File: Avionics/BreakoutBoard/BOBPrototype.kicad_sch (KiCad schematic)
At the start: 0 parts

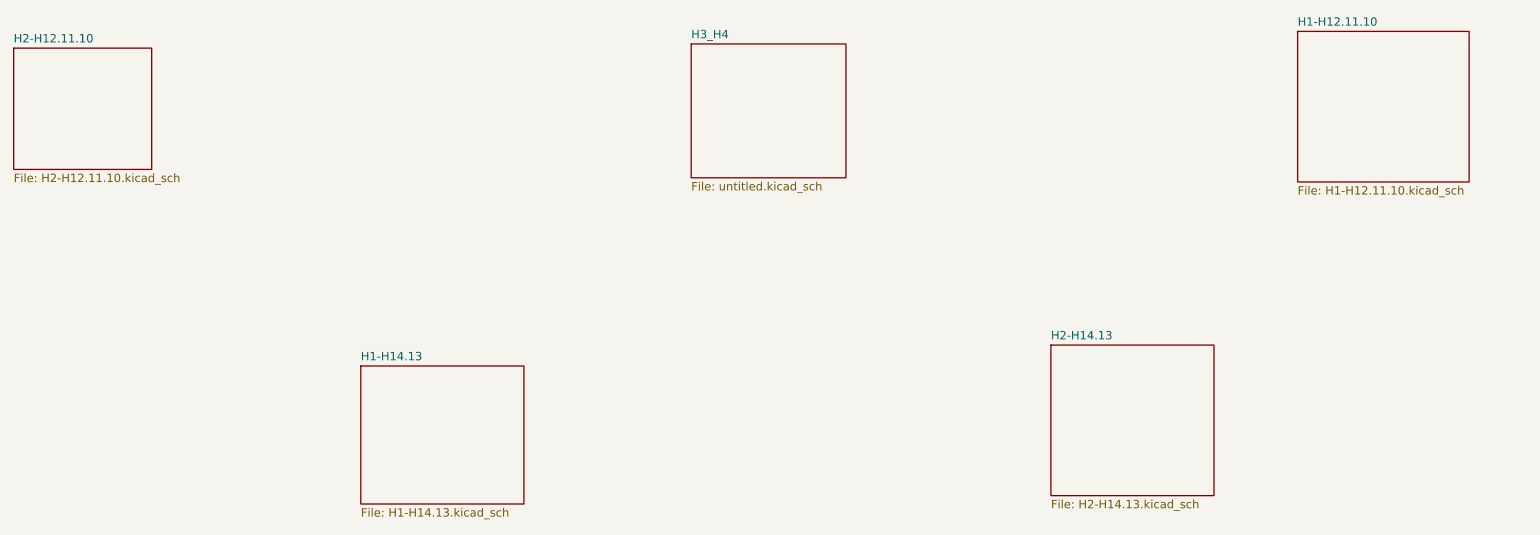
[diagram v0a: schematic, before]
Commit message: Add files via upload
Sephora Poteau, updates:
- Adding where power is presumed to come from
- Added where pins should be connected to GND on H3 and H4
- Changed layout of H1 and H2 so that all symbols would be on one sheet
- Adding footprints to all symbols
- Created outline for board according to PC104 standards
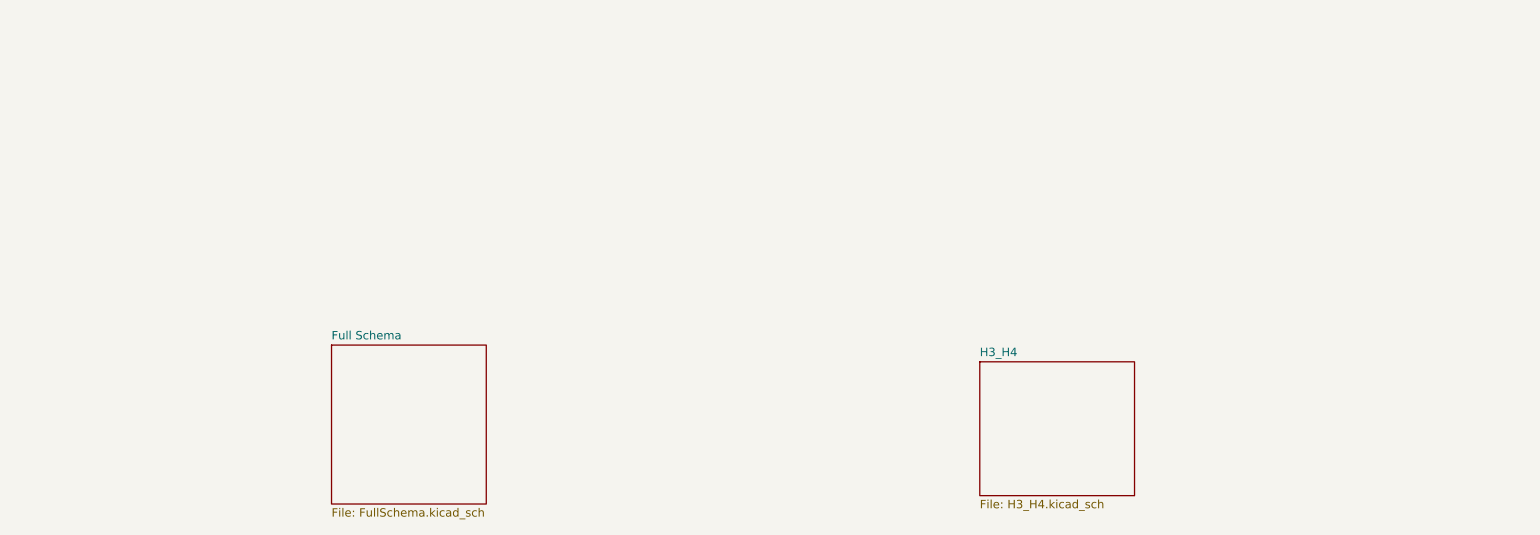
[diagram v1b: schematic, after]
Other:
- removed sheet H1-H12.11.10
- removed sheet H1-H14.13
- removed sheet H2-H12.11.10
- removed sheet H2-H14.13
- added sheet Full Schema (FullSchema.kicad_sch)
- sheet H3_H4: file untitled.kicad_sch -> H3_H4.kicad_sch
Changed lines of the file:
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@@
 	(paper "A4")
 	(sheet
-		(at 135.255 28.575)
+		(at 179.07 76.835)
 		(size 23.495 20.32)
 		(fields_autoplaced yes)
@@
 		)
 		(property "Sheetname" "H3_H4"
-			(at 135.255 27.8634 0)
+			(at 179.07 76.1234 0)
 			(effects
 				(font
@@
 			)
 		)
-		(property "Sheetfile" "untitled.kicad_sch"
-			(at 135.255 49.4796 0)
-			(effects
-				(font
-					(size 1.27 1.27)
-				)
-				(justify left top)
-			)
-		)
-		(instances
-			(project "BOBPrototype"
-				(path "/4940c63c-65b5-4f17-bae9-f8f159cf243f"
-					(page "6")
-				)
-			)
-		)
-	)
-	(sheet
-		(at 227.33 26.67)
-		(size 26.035 22.86)
-		(fields_autoplaced yes)
-		(stroke
-			(width 0.1524)
-			(type solid)
-		)
-		(fill
-			(color 0 0 0 0.0000)
-		)
-		(property "Sheetname" "H1-H12.11.10"
-			(at 227.33 25.9584 0)
-			(effects
-				(font
-					(size 1.27 1.27)
-				)
-				(justify left bottom)
-			)
-		)
-		(property "Sheetfile" "H1-H12.11.10.kicad_sch"
-			(at 227.33 50.1146 0)
-			(effects
-				(font
-					(size 1.27 1.27)
-				)
-				(justify left top)
-			)
-		)
-		(instances
-			(project "BOBPrototype"
-				(path "/4940c63c-65b5-4f17-bae9-f8f159cf243f"
-					(page "2")
-				)
-			)
-		)
-	)
-	(sheet
-		(at 85.09 77.47)
-		(size 24.765 20.955)
-		(fields_autoplaced yes)
-		(stroke
-			(width 0.1524)
-			(type solid)
-		)
-		(fill
-			(color 0 0 0 0.0000)
-		)
-		(property "Sheetname" "H1-H14.13"
-			(at 85.09 76.7584 0)
-			(effects
-				(font
-					(size 1.27 1.27)
-				)
-				(justify left bottom)
-			)
-		)
-		(property "Sheetfile" "H1-H14.13.kicad_sch"
-			(at 85.09 99.0096 0)
+		(property "Sheetfile" "H3_H4.kicad_sch"
+			(at 179.07 97.7396 0)
 			(effects
 				(font
@@
 	)
 	(sheet
-		(at 32.385 29.21)
-		(size 20.955 18.415)
+		(at 80.645 74.295)
+		(size 23.495 24.13)
 		(fields_autoplaced yes)
 		(stroke
@@
 			(color 0 0 0 0.0000)
 		)
-		(property "Sheetname" "H2-H12.11.10"
-			(at 32.385 28.4984 0)
+		(property "Sheetname" "Full Schema"
+			(at 80.645 73.5834 0)
 			(effects
 				(font
@@
 			)
 		)
-		(property "Sheetfile" "H2-H12.11.10.kicad_sch"
-			(at 32.385 48.2096 0)
+		(property "Sheetfile" "FullSchema.kicad_sch"
+			(at 80.645 99.0096 0)
 			(effects
 				(font
@@
 			(project "BOBPrototype"
 				(path "/4940c63c-65b5-4f17-bae9-f8f159cf243f"
-					(page "4")
+					(page "2")
 				)
 			)
-		)
-	)
-	(sheet
-		(at 189.865 74.295)
-		(size 24.765 22.86)
-		(fields_autoplaced yes)
-		(stroke
-			(width 0.1524)
-			(type solid)
-		)
-		(fill
-			(color 0 0 0 0.0000)
-		)
-		(property "Sheetname" "H2-H14.13"
-			(at 189.865 73.5834 0)
-			(effects
-				(font
-					(size 1.27 1.27)
-				)
-				(justify left bottom)
-			)
-		)
-		(property "Sheetfile" "H2-H14.13.kicad_sch"
-			(at 189.865 97.7396 0)
-			(effects
-				(font
-					(size 1.27 1.27)
-				)
-				(justify left top)
-			)
-		)
-		(instances
-			(project "BOBPrototype"
-				(path "/4940c63c-65b5-4f17-bae9-f8f159cf243f"
-					(page "5")
-				)
-			)
